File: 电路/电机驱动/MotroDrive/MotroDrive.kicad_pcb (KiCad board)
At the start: 2 copper layers, 33 x 48 mm, 20 parts, among them J1 Conn_01x04_MountingPin, J2 Conn_01x02_MountingPin, U1 TLV61048DBVR

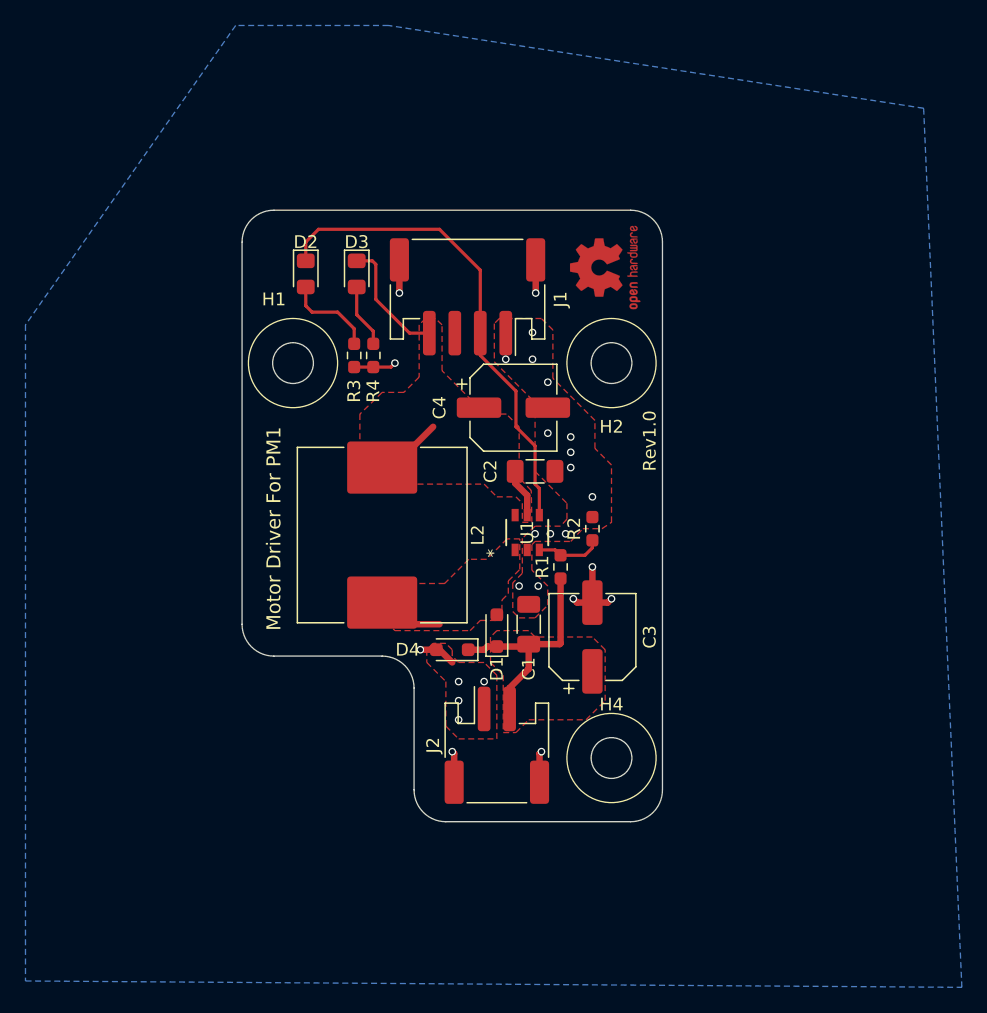
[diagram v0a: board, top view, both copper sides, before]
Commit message: 主控升级至Rev1.2，电机驱动 Rev1.1
电机驱动修改后采用Mosfet控制高侧电源通路。主控配套进行了更改。
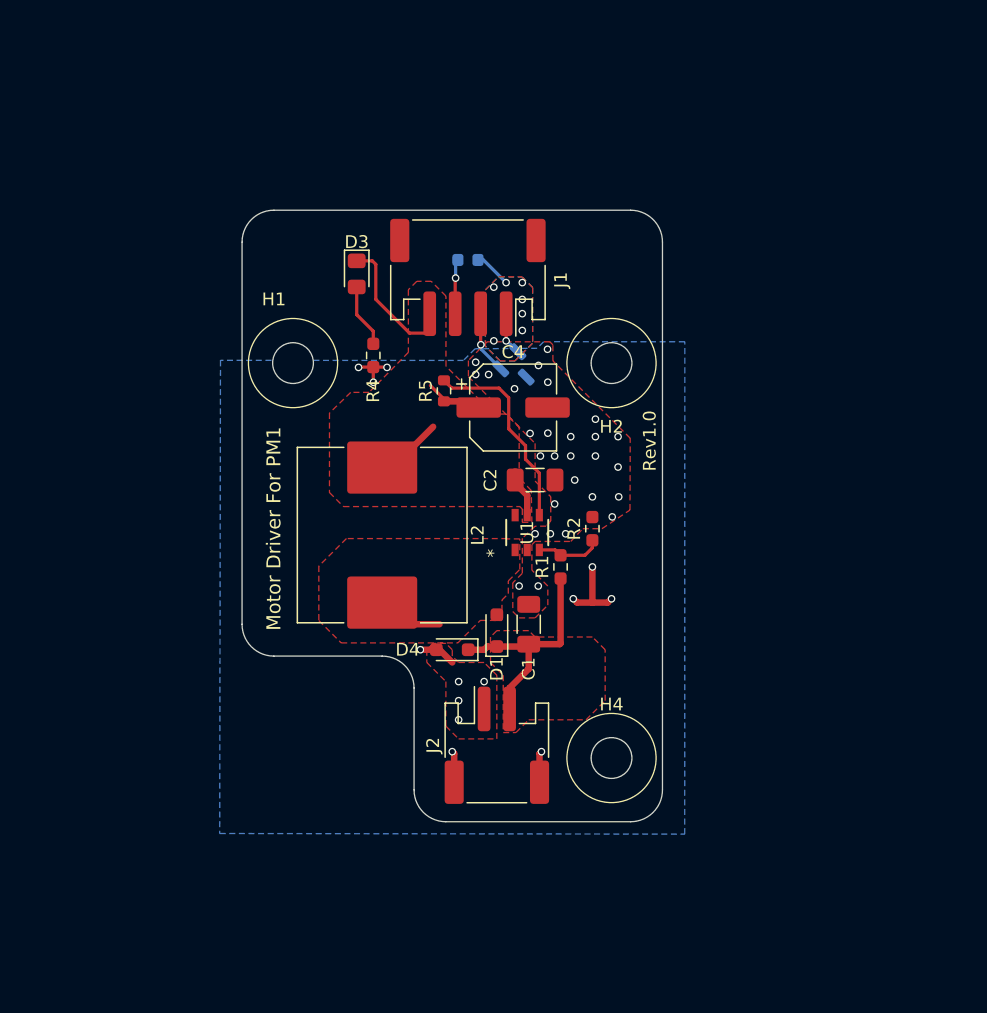
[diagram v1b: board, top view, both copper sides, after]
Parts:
- removed C3: 100uf, Capacitor_SMD:CP_Elec_6.3x7.7
- removed D2: LED, LED_SMD:LED_0805_2012Metric_Pad1.15x1.40mm_HandSolder
- removed R3: 10k, Resistor_SMD:R_0603_1608Metric_Pad0.98x0.95mm_HandSolder
- removed REF1: OSHW-Logo2_7.3x6mm_Copper, Symbol:OSHW-Logo2_7.3x6mm_Copper
- added FB1: FerriteBead, Inductor_SMD:L_0603_1608Metric, B.Cu at (72.7, 45.9)
- added Q1: AO3400A, Package_TO_SOT_SMD:SOT-23, B.Cu at (76.6, 54.4)
- added R5: 1k, Resistor_SMD:R_0603_1608Metric, F.Cu at (70.8, 56.2)
- moved J1 1.52 mm to (72.7, 47.3)
- moved C2 0.68 mm to (78.0, 63.2)
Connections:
- J1 pad 1: GND -> /POWER_GND
- J1 pad 2: /MoterEN -> /MT_EN
- J1 pad 3: unconnected-(J1-Pin_3-Pad3) -> Net-(J1-Pin_3)
- J1 pad MP: GND -> unconnected-(J1-MountPin-PadMP)
- U1 pad 4: /MoterEN -> Net-(U1-EN)
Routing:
- net /MoterEN: track 38.1 -> 0.00 mm
- net Net-(U1-EN): track 0.00 -> 15.9 mm
- net Net-(D2-A): track 7.21 -> 0.00 mm
- net /POWER_GND: track 0.00 -> 6.35 mm, vias 0 -> 8
- net GND: track 22.4 -> 17.3 mm, vias 27 -> 41
- net /MT_EN: track 0.00 -> 4.97 mm, vias 0 -> 1
- net +BATT: track 18.8 -> 23.4 mm
- net Net-(J1-Pin_3): track 0.00 -> 4.31 mm, vias 0 -> 1
- added copper zone on B.Cu, net /POWER_GND
- added copper zone on F.Cu, net /POWER_GND

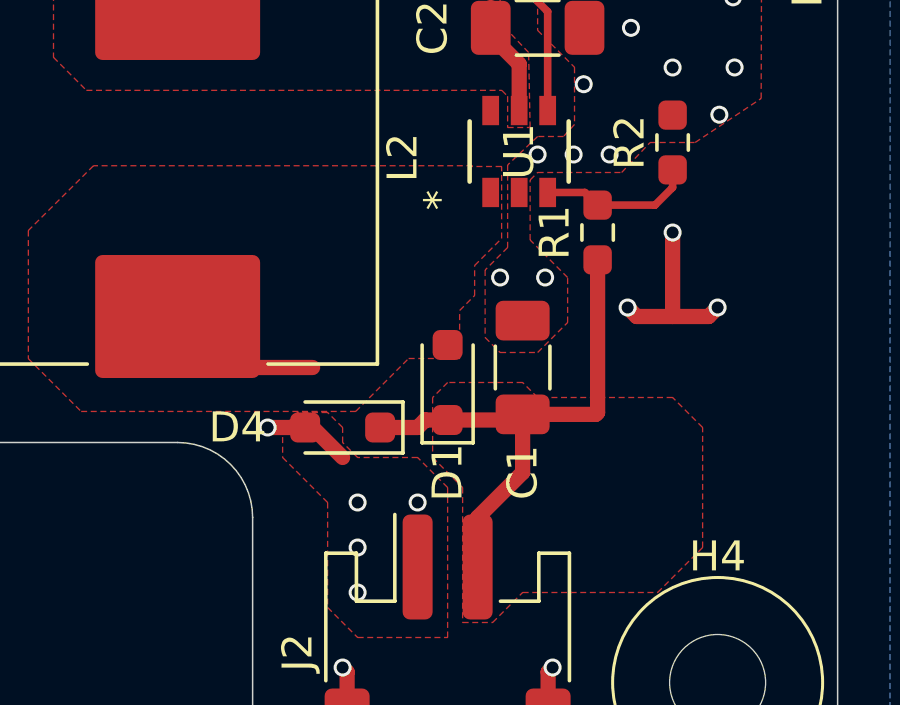
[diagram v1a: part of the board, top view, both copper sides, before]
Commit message: 原本齿轮定位尺寸ok不应再加高度；修改电机驱动电路，但是电机驱动电路未完全ok
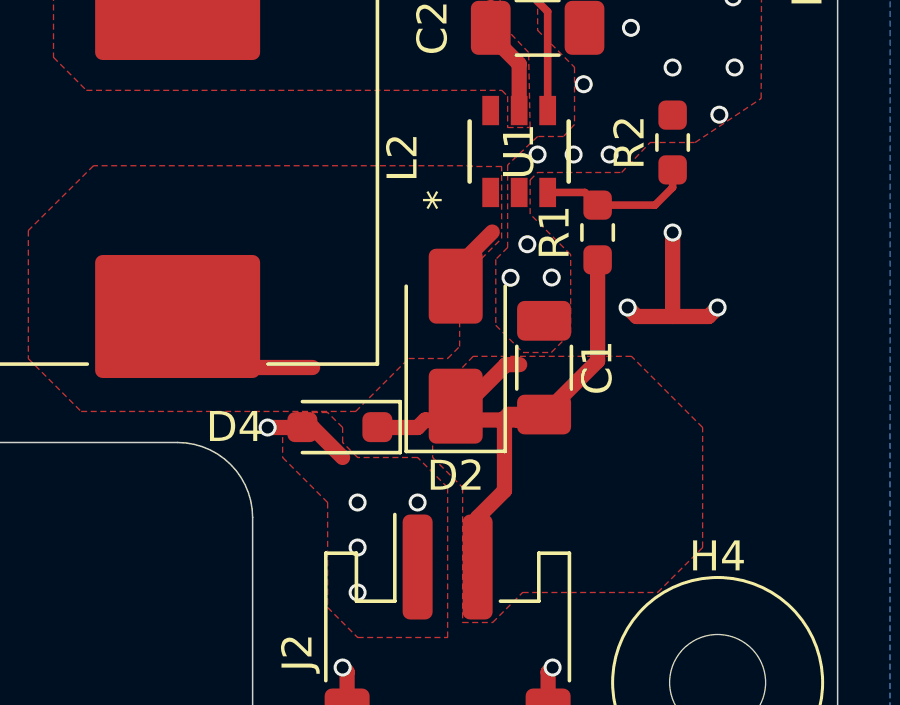
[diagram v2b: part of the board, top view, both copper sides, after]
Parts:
- removed D1: 1N5819WS, Diode_SMD:D_SOD-323_HandSoldering
- added D2: SS34, Diode_SMD:D_SMA, F.Cu at (75.3, 73.8)
- moved C1 0.72 mm to (78.2, 74.5)
- moved D4 0.09 mm to (71.4, 76.5)
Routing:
- net /Motor+: track 19.3 -> 21.9 mm
- net /SW: track 5.20 -> 7.51 mm
- net GND: vias 41 -> 42

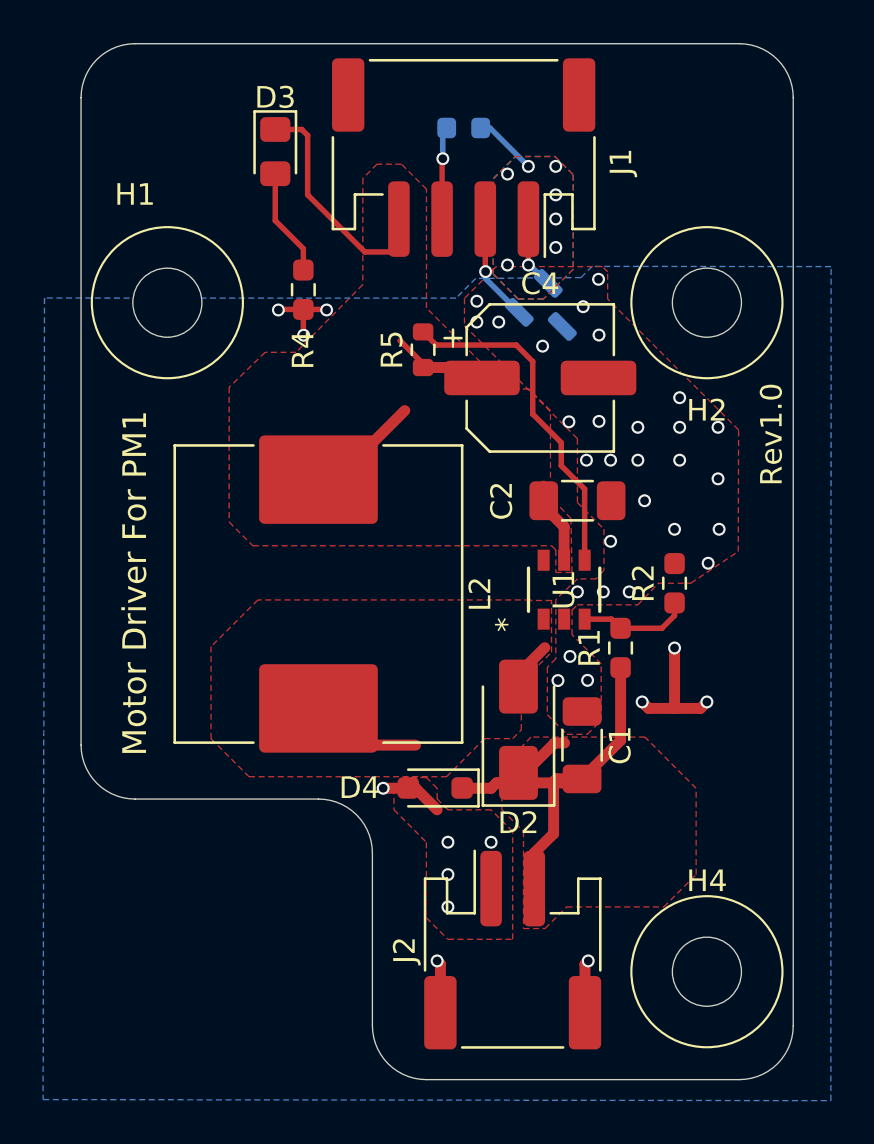
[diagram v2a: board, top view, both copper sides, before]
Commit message: 驱动电路升级至R1.2 未验证
R1.2 升压二极管改为SS34；储能电容改为连接原始电源GND；电路板改为单面布局
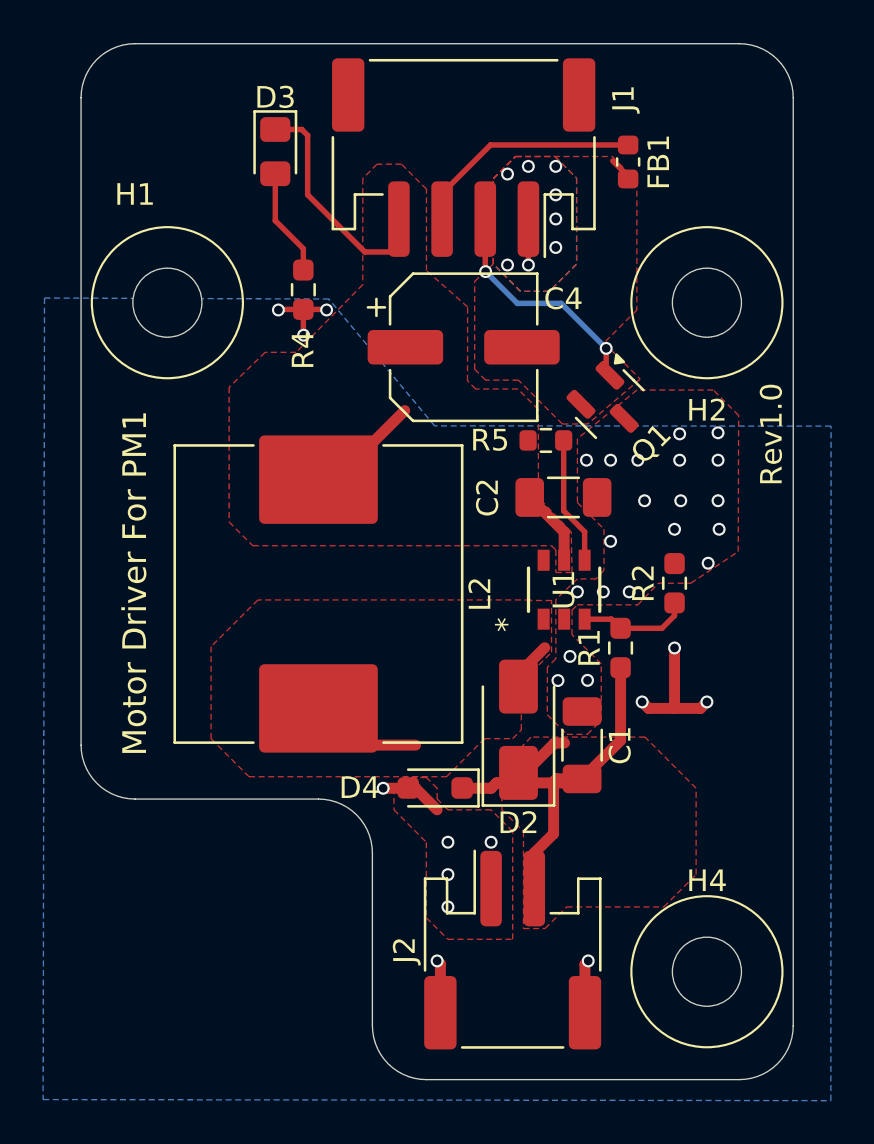
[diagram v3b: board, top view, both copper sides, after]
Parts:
- FB1, Q1: moved to F.Cu
- moved FB1 7.78 mm to (80.3, 47.5), turned to -90 degrees
- moved R5 7.07 mm to (76.5, 60.4), turned to 0 degrees
- moved Q1 5.13 mm to (79.5, 58.7)
- moved C4 3.82 mm to (72.7, 56.1)
- moved C2 0.67 mm to (77.4, 63.0)
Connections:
- C4 pad 2: GND -> /POWER_GND
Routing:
- net Net-(U1-EN): track 15.9 -> 5.95 mm
- net Net-(J1-Pin_3): track 4.31 -> 10.7 mm, vias 1 -> 0
- net /MT_EN: track 4.97 -> 10.8 mm, vias 1 -> 2
- net +BATT: track 23.4 -> 18.5 mm
- net /POWER_GND: track 6.35 -> 3.26 mm
- net GND: vias 42 -> 33
